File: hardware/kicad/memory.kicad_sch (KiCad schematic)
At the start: 8 parts, among them U6 Address_Decoder, U7 AS6C4008, U8 AS6C4008, U9 AT28C256

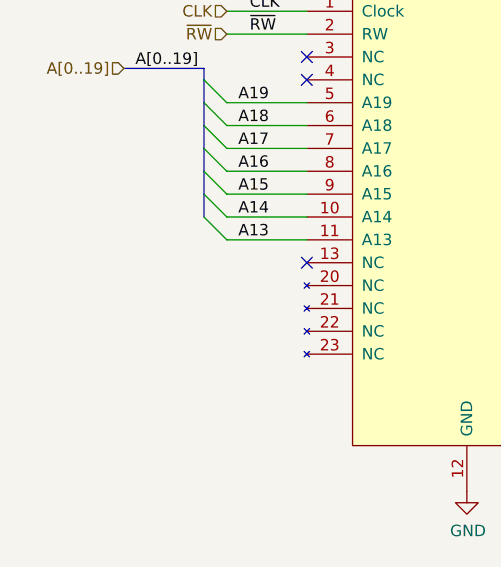
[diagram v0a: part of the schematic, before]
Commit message: update hardware files to match current WIP design
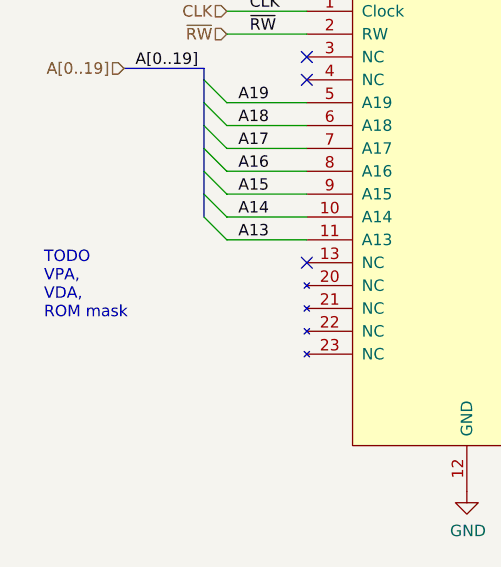
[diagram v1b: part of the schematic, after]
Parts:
- C6, C7, C8, C9: footprint (none) -> Capacitor_SMD:C_0603_1608Metric_Pad1.08x0.95mm_HandSolder
- U6: footprint (none) -> Package_DIP:DIP-24_W7.62mm_Socket
- U7, U8: footprint (none) -> Package_DIP:DIP-32_W15.24mm_Socket
- U9: footprint (none) -> Package_DIP:DIP-28_W15.24mm_Socket
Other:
- note added: "TODO VPA, VDA, ROM mask"
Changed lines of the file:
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@@
     (stroke (width 0) (type default) (color 0 0 0 0))
+  )
+  (text "TODO\nVPA,\nVDA,\nROM mask" (at 19.05 76.2 0)
+    (effects (font (size 1.27 1.27)) (justify left bottom))
   )
   (text "ROM" (at 55.88 118.11 0)
@@
     (property "Reference" "U9" (id 0) (at 64.77 121.1326 0))
     (property "Value" "AT28C256" (id 1) (at 64.77 123.444 0))
-    (property "Footprint" "" (id 2) (at 64.77 153.67 0)
+    (property "Footprint" "Package_DIP:DIP-28_W15.24mm_Socket" (id 2) (at 64.77 153.67 0)
       (effects (font (size 1.27 1.27)) hide)
     )
@@
     (property "Reference" "U7" (id 0) (at 156.21 28.4226 0))
     (property "Value" "AS6C4008" (id 1) (at 156.21 30.734 0))
-    (property "Footprint" "" (id 2) (at 156.21 60.96 0)
+    (property "Footprint" "Package_DIP:DIP-32_W15.24mm_Socket" (id 2) (at 156.21 60.96 0)
       (effects (font (size 1.27 1.27)) hide)
     )
@@
       (effects (font (size 1.27 1.27)) (justify left))
     )
-    (property "Footprint" "" (id 2) (at 126.6952 182.88 0)
+    (property "Footprint" "Capacitor_SMD:C_0603_1608Metric_Pad1.08x0.95mm_HandSolder" (id 2) (at 126.6952 182.88 0)
       (effects (font (size 1.27 1.27)) hide)
     )
@@
       (effects (font (size 1.27 1.27)) (justify left))
     )
-    (property "Footprint" "" (id 2) (at 139.3952 182.88 0)
+    (property "Footprint" "Capacitor_SMD:C_0603_1608Metric_Pad1.08x0.95mm_HandSolder" (id 2) (at 139.3952 182.88 0)
       (effects (font (size 1.27 1.27)) hide)
     )
@@
       (effects (font (size 1.27 1.27)) (justify left))
     )
-    (property "Footprint" "" (id 2) (at 152.0952 182.88 0)
+    (property "Footprint" "Capacitor_SMD:C_0603_1608Metric_Pad1.08x0.95mm_HandSolder" (id 2) (at 152.0952 182.88 0)
       (effects (font (size 1.27 1.27)) hide)
     )
@@
       (effects (font (size 1.27 1.27)) (justify left))
     )
-    (property "Footprint" "" (id 2) (at 164.7952 182.88 0)
+    (property "Footprint" "Capacitor_SMD:C_0603_1608Metric_Pad1.08x0.95mm_HandSolder" (id 2) (at 164.7952 182.88 0)
       (effects (font (size 1.27 1.27)) hide)
     )
@@
     (property "Reference" "U8" (id 0) (at 231.14 29.6926 0))
     (property "Value" "AS6C4008" (id 1) (at 231.14 32.004 0))
-    (property "Footprint" "" (id 2) (at 231.14 62.23 0)
+    (property "Footprint" "Package_DIP:DIP-32_W15.24mm_Socket" (id 2) (at 231.14 62.23 0)
       (effects (font (size 1.27 1.27)) hide)
     )
@@
       (effects (font (size 1.524 1.524)) (justify left))
     )
-    (property "Footprint" "" (id 2) (at 52.07 40.64 0)
+    (property "Footprint" "Package_DIP:DIP-24_W7.62mm_Socket" (id 2) (at 52.07 40.64 0)
       (effects (font (size 1.524 1.524)) (justify right) hide)
     )

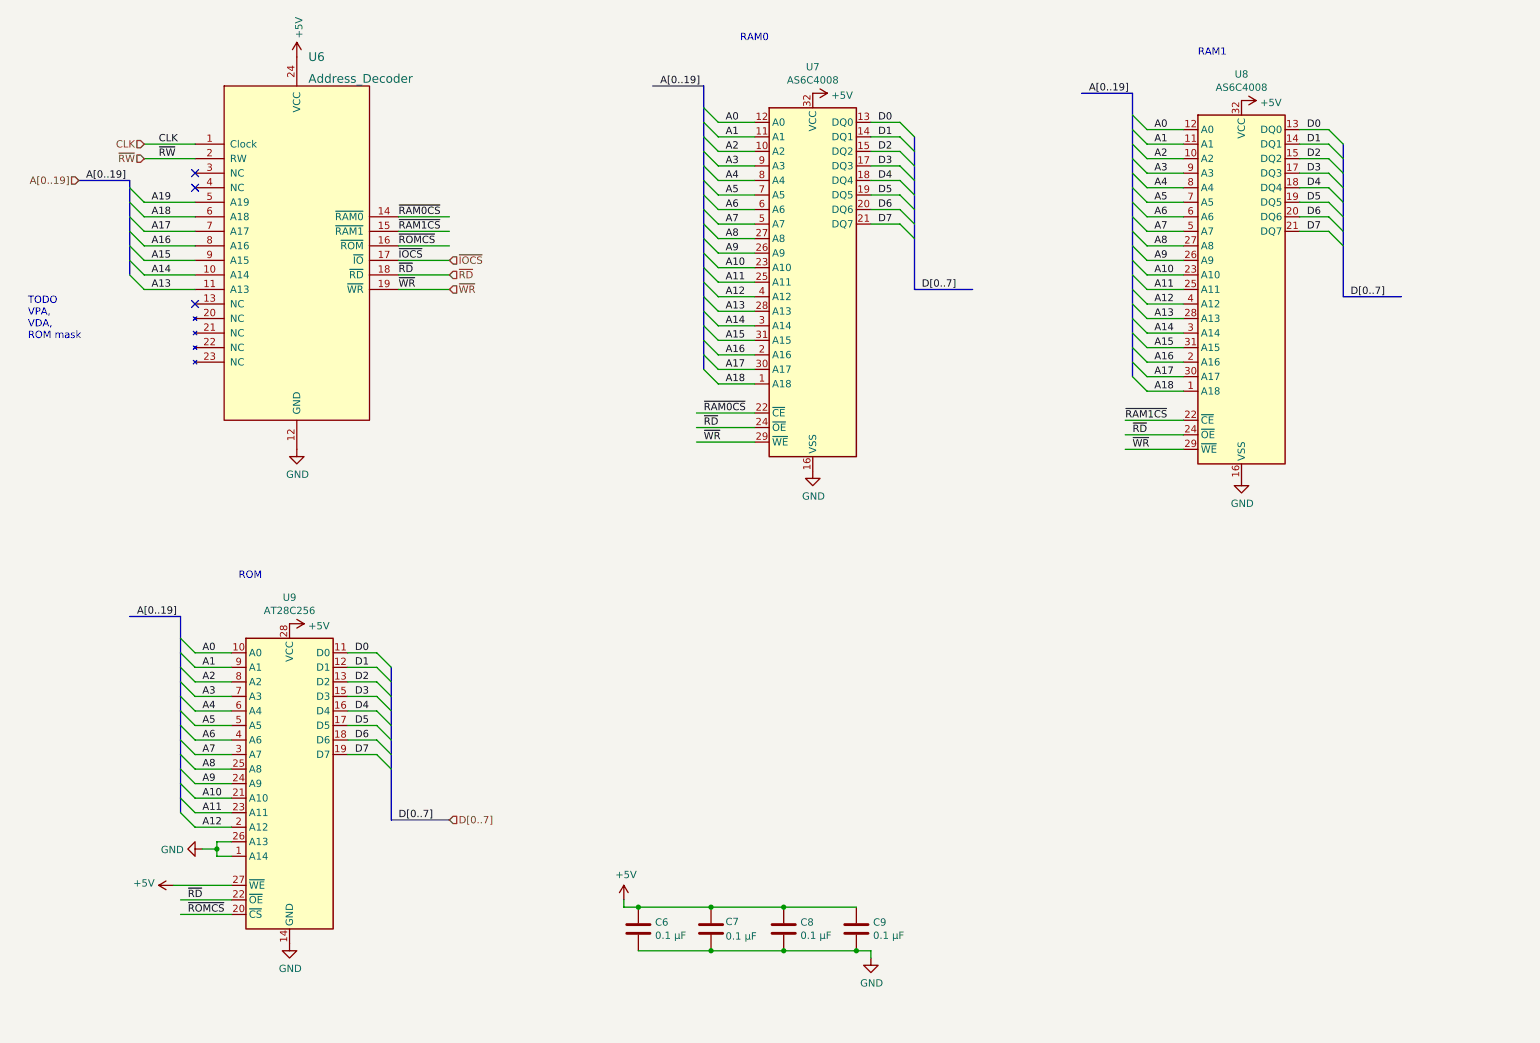
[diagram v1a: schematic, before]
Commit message: update schematic, add draft PCB
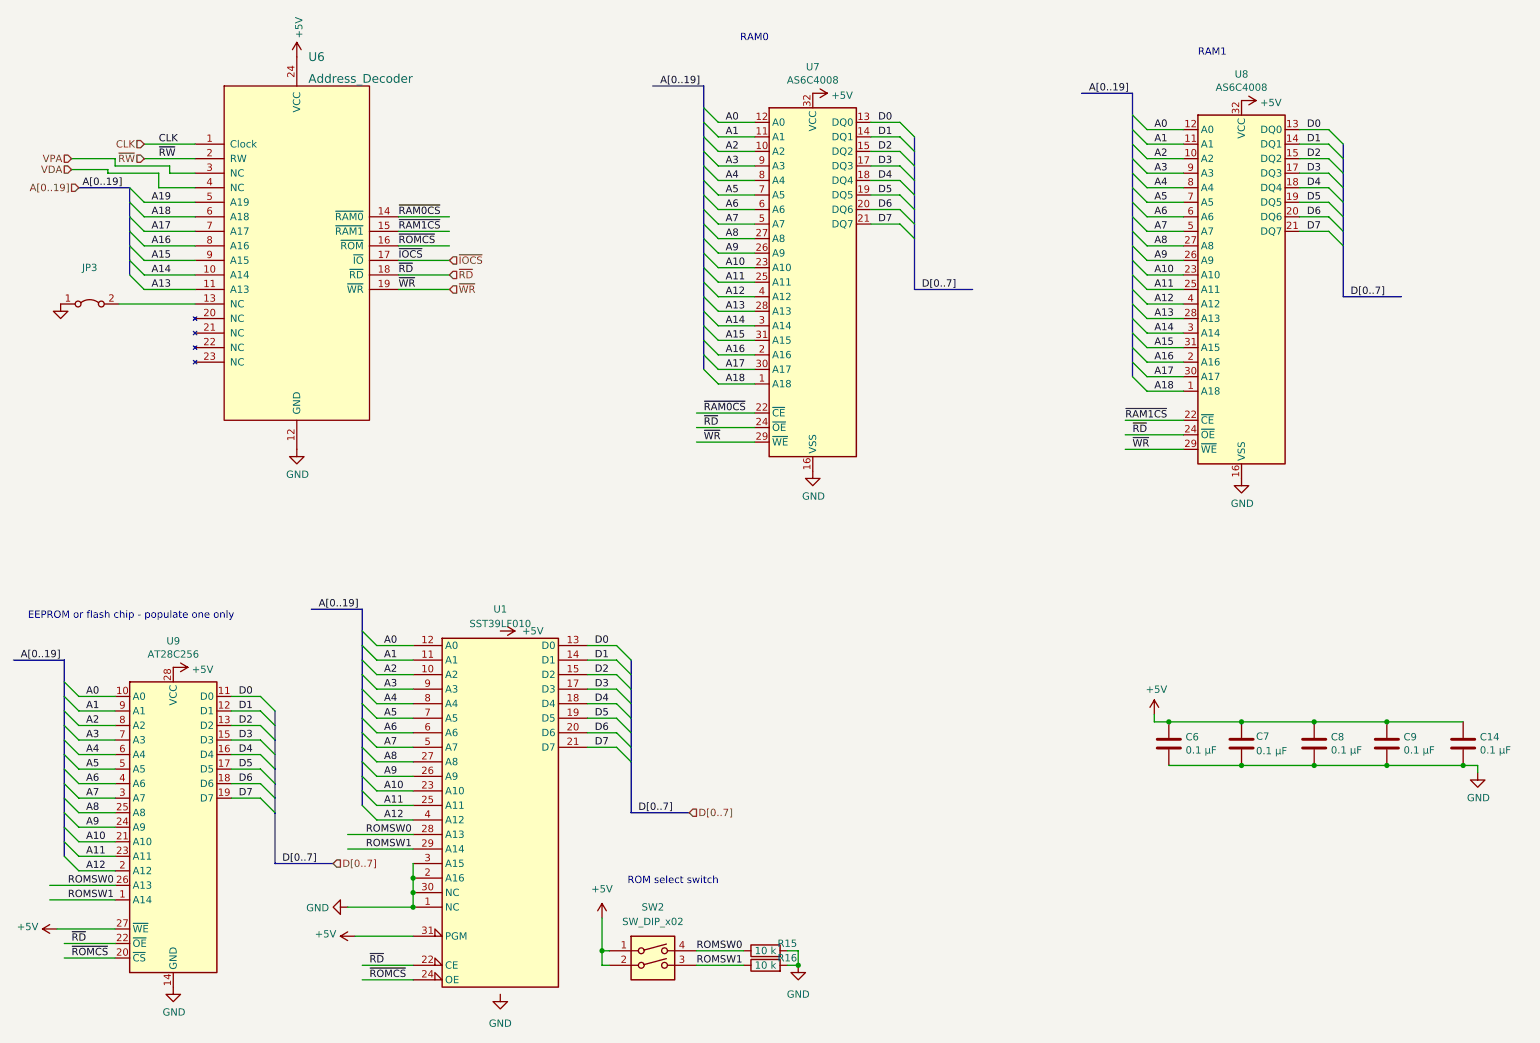
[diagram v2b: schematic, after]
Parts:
- added C14: 0.1 µF, Capacitor_SMD:C_0603_1608Metric_Pad1.08x0.95mm_HandSolder, symbol Device:C
- added JP3: (no value), symbol Jumper:Jumper_2_Bridged
- added R15, R16: 10 k, Resistor_SMD:R_0603_1608Metric_Pad0.98x0.95mm_HandSolder, symbol Device:R
- added SW2: SW_DIP_x02, Button_Switch_SMD:SW_DIP_SPSTx02_Slide_6.7x6.64mm_W8.61mm_P2.54mm_LowProfile, symbol Switch:SW_DIP_x02
- added U1: SST39LF010, Package_LCC:PLCC-32_11.4x14.0mm_P1.27mm, symbol Memory_Flash:SST39SF010
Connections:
- net +5V: now also C14.1, SW2.1, SW2.2, U1.31 (PGM), U1.32 (VCC)
- net A0: now also U1.12 (A0)
- net A1: now also U1.11 (A1)
- net A10: now also U1.23 (A10)
- net A11: now also U1.25 (A11)
- net A12: now also U1.4 (A12)
- net A2: now also U1.10 (A2)
- net A3: now also U1.9 (A3)
- net A4: now also U1.8 (A4)
- net A5: now also U1.7 (A5)
- net A6: now also U1.6 (A6)
- net A7: now also U1.5 (A7)
- net A8: now also U1.27 (A8)
- net A9: now also U1.26 (A9)
- net D0: now also U1.13 (D0)
- net D1: now also U1.14 (D1)
- net D2: now also U1.15 (D2)
- net D3: now also U1.17 (D3)
- net D4: now also U1.18 (D4)
- net D5: now also U1.19 (D5)
- net D6: now also U1.20 (D6)
- net D7: now also U1.21 (D7)
- net GND: now also C14.2, JP3.1 (A), R15.2, R16.2, U1.1 (NC), U1.16 (GND), U1.2 (A16), U1.3 (A15), U1.30 (NC); no longer U9.1 (A14), U9.26 (A13)
- net ~{RD}: now also U1.22 (CE)
- net ~{ROMCS}: now also U1.24 (OE)
- net at U6.13 (NC): now also JP3.2 (B)
- net VPA: now reaches U6.3 (NC)
- net VDA: now reaches U6.4 (NC)
- new net ROMSW0: R15.1, SW2.4, U1.28 (A13), U9.26 (A13)
- new net ROMSW1: R16.1, SW2.3, U1.29 (A14), U9.1 (A14)
- no-connect marks 3 -> 0
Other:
- note added: "EEPROM or flash chip - populate one only"
- note added: "ROM select switch"
- note removed: "ROM"
- note removed: "TODO VPA, VDA, ROM mask"
- moved on the sheet: C6, C7, C8, C9, U9

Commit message: pcb updates
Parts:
- added J16: Conn_01x06, Connector_PinHeader_2.54mm:PinHeader_1x06_P2.54mm_Vertical, symbol Connector_Generic:Conn_01x06
- added J17: Conn_01x04, Connector_PinHeader_2.54mm:PinHeader_1x04_P2.54mm_Vertical, symbol Connector_Generic:Conn_01x04
- JP3: value (none) -> Jumper_2_Bridged; footprint (none) -> Connector_PinHeader_2.54mm:PinHeader_1x02_P2.54mm_Vertical
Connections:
- net ~{IOCS}: now also J16.4 (Pin_4)
- net ~{RAM0CS}: now also J16.1 (Pin_1)
- net ~{RAM1CS}: now also J16.2 (Pin_2)
- net ~{RD}: now also J16.5 (Pin_5)
- net ~{ROMCS}: now also J16.3 (Pin_3)
- net ~{WR}: now also J16.6 (Pin_6)
- net S0: now reaches JP3.2 (B), U6.13 (S0)
- net S1: now reaches U6.20 (S1)
- net S1: now also J17.1 (Pin_1)
- net S2: now reaches U6.21 (S2)
- net S2: now also J17.2 (Pin_2)
- net S3: now reaches U6.22 (S3)
- net S3: now also J17.3 (Pin_3)
- net S4: now reaches U6.23 (S4)
- net S4: now also J17.4 (Pin_4)
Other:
- note added: "Address decode expansion headers"
